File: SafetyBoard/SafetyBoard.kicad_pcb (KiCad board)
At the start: 2 copper layers, 169 parts, among them J1 ESTOP/SDC switch, J10 Dash, J11 BBC, J12 614004135023, J13 RTD B, J14 Brakelight, J15 SHOCK/WHEEL SNSR, J16 footwell, J18 AMP, J19 39306207, J2 SDC OUT, J3 ACCU, J4 12v EXP, J5 PWR IN, J6 24v EXP, J7 5v EXP, J8 Current Sensor, J9 TSSI, K1 G6B-2214P-US DC12, K2 G6B-2214P-US DC12, K3 G6B-2214P-US DC12, Q1 IRLIZ44N NMOS, Q2 IRLIZ44N NMOS, Q3 IRLIZ44N NMOS, Q4 IRLIZ44N NMOS, Q5 PMOS IRF9540, Q6 PMOS IRF9540, Q7 PMOS IRF9540, SW1 SW_Push, SW2 SW_Push, SW3 SW_Push, U1 40106 Inverter, U2 4081 AND Gate, U3 LT1084-5.0, U4 LM393, U5 LM393, U6 4071 4 Channel 2 Input OR gate, U7 LM393, U8 LM555xN, U9 OKX-T/5-D12N-C

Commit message: silkscreen and some fuses or something
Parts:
- removed the D1 at (177.2, 82.0)
- removed the D5 at (271.4, 67.4)
- removed FL1: RGF48040A-001, DCDCfootprints:EMI Filter RGF48040A001
- added C27: 1u, Capacitor_SMD:C_0805_2012Metric, B.Cu at (186.5, 125.1)
- added C30: 1u, Capacitor_SMD:C_0805_2012Metric, B.Cu at (155.0, 142.5)
- added D2: D, Diode_SMD:D_0603_1608Metric, B.Cu at (140.3, 95.5)
- added D7: D, Diode_SMD:D_0603_1608Metric, B.Cu at (148.4, 78.2)
- added R55: ~, Resistor_SMD:R_0805_2012Metric, B.Cu at (154.7, 147.5)
- added R56: 10k, Resistor_SMD:R_0603_1608Metric, B.Cu at (120.0, 74.5)
- C26, C4, LED1, R22, R25, R26, R27, R35, R36, R37, R_Bypass1, R_Bypass2: moved to B.Cu
- D12: renamed from D10; moved to B.Cu
- D3: value RF01VM2S -> D; footprint Diode_SMD:D_0805_2012Metric -> Diode_SMD:D_0603_1608Metric; moved to B.Cu
- D4: value RF01VM2S -> ON when ok; footprint Diode_SMD:D_0805_2012Metric -> LED_THT:LED_D5.0mm
- F1, F5: value ~ -> 2A MAX
- F10, F3, F6, F7: value ~ -> 5A MAX
- F11: renamed from F12; value ~ -> 3A
- F4, F8, F9: value ~ -> 10A MAX
- Q2, Q3: moved to F.Cu
- R29: renamed from R28; moved to B.Cu
- R30: renamed from R29; moved to B.Cu
- R31: renamed from R30; moved to B.Cu
- R34: renamed from R33; moved to B.Cu
- R38: renamed from R40; moved to B.Cu
- R39: renamed from R41; moved to B.Cu
- R41: renamed from R45; moved to B.Cu
- R42: renamed from R46; moved to B.Cu
- R43: renamed from R47; moved to B.Cu
- R49: renamed from R54; moved to B.Cu
- U6: value 4071 4 Channel 2 Input OR gate -> CD4071BE OR Gate
- moved F1 490.8 mm to (191.1, 121.6), turned to 90 degrees
- moved H1 341.8 mm to (318.5, 132.4)
- moved H2 341.8 mm to (318.5, 140.0)
- moved H3 341.8 mm to (318.5, 147.5)
- moved H4 341.8 mm to (318.5, 155.1)
- moved H5 248.9 mm to (368.4, 72.9)
- moved H7 248.9 mm to (368.4, 88.8)
- moved H8 248.9 mm to (368.4, 96.7)
- moved H6 248.9 mm to (368.4, 80.8)
- moved F5 241.6 mm to (208.3, 129.2), turned to 90 degrees
- moved F2 206.5 mm to (196.4, 132.0), turned to -90 degrees
- moved R38 182.8 mm to (176.0, 86.3)
- moved R39 179.6 mm to (183.4, 95.0)
- moved R42 173.6 mm to (197.0, 86.3), turned to 90 degrees
- moved R27 171.8 mm to (141.2, 92.9), turned to 90 degrees
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- renumbered LED3 to BothThreshold1, C27 to C28, C32 to C29, C28 to C31, C29 to C32, C30 to C33, C31 to C34, D2 to D1, D11 to D10, D12 to D11, D6 to D5, D7 to D6, D9 to D8, D8 to D9, F11 to F12, J16 to J13, J13 to J14, J14 to J15, J15 to J16, J19 to J17, LED2 to OutOfRange1, R34 to R28, R31 to R32, R32 to R33, R42 to R40, R49 to R44, R50 to R45, R51 to R46, R52 to R47, R53 to R48, R55 to R50, R56 to R51, R57 to R52, R58 to R53, R59 to R54
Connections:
- C20 pad 1: Net-(FL1-CASE) -> /24V
- C21 pad 1: Net-(FL1-VOUT(+)_) -> /24V
- C22 pad 1: Net-(FL1-VOUT(+)_) -> /24V
- D3 pad 1: Net-(D3-K) -> Net-(D2-K)
- D3 pad 2: /LATCH/bms_imd_latch_only -> Net-(D3-A)
- D4 pad 1: Net-(D3-K) -> GND
- F1 pad 1: +12V -> /12V
- F1 pad 2: /12V -> +12V
- J13 pad 4: unconnected-(J16-Pad4) -> /CCM Helper/CCM3v3
- J17 pad 10: unconnected-(J19-Pad10) -> /CCM Helper/24V
- J17 pad 11: unconnected-(J19-Pad11) -> /CCM Helper/RTDB
- J17 pad 12: /CCM Helper/CCMGND -> GND
- J17 pad 13: unconnected-(J19-Pad13) -> /CCM Helper/5V
- J17 pad 19: unconnected-(J19-Pad19) -> /CCM Helper/Brakelight
- J17 pad 20: /CCM Helper/Brakelight -> /CCM Helper/12V
- J17 pad 4: /CCM Helper/24V -> /CCM Helper/CCMGND
- J2 pad 1: Net-(J1-Pin_2) -> unconnected-(J2-Pin_1-Pad1)
- K1 pad 3: /LATCH/bms_imd_latch_only -> /LATCH/GVLM_OUTPUT
- K1 pad 4: /LATCH/GVLM_OUTPUT -> /LATCH/bms_imd_latch_only
- K2 pad 3: Net-(K2-Pad3) -> /LATCH/bms_imd_latch_only
- K2 pad 4: /LATCH/bms_imd_latch_only -> Net-(K2-Pad4)
- K3 pad 4: Net-(K2-Pad3) -> Net-(K2-Pad4)
- PS1 pad 1: Net-(FL1-VOUT(+)_) -> /24V
- PS1 pad 5: unconnected-(PS1-CURRENT_LIMIT_(OCP)_ADJUST-Pad5) -> Net-(PS1-CURRENT_LIMIT_(OCP)_ADJUST)
- PS1 pad 9: Net-(FL1-VOUT(+)_) -> /24V
- Q2 pad 2: GND -> Net-(D3-A)
- Q2 pad 3: Net-(D4-A) -> GND
- Q3 pad 1: Net-(D3-K) -> Net-(D2-K)
- R26 pad 2: Net-(D4-A) -> Net-(D3-A)
- R28 pad 1: Net-(D3-K) -> Net-(D2-K)
- R30 pad 1: Net-(D3-K) -> Net-(D2-K)
- R30 pad 2: Net-(D5-A) (its old number) -> Net-(D4-A)
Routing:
- net +12V: track 35.0 -> 262.4 mm, vias 0 -> 15
- net /CCM Helper/12V: track 0.00 -> 185.9 mm
- net Net-(J1-Pin_2): track 0.00 -> 174.9 mm, vias 0 -> 10
- net Net-(J3-Pin_1): track 0.00 -> 169.2 mm, vias 0 -> 5
- net Net-(D2-K): track 0.00 -> 137.1 mm, vias 0 -> 1
- net /TSSI/GLV: track 0.00 -> 123.2 mm, vias 0 -> 3
- net /BSPD/B_IN: track 0.00 -> 74.3 mm, vias 0 -> 2
- net /5V: track 0.00 -> 72.8 mm, vias 0 -> 1
- net /CCM Helper/CCM fdbk: track 0.00 -> 66.0 mm, vias 0 -> 1
- net /TSSI/GREEN_LED: track 0.00 -> 65.8 mm
- net /LATCH/bspd_reset: track 0.00 -> 65.6 mm, vias 0 -> 2
- net /CCM Helper/24V: track 0.00 -> 63.4 mm
- net /CCM Helper/CCMGND: track 0.00 -> 62.4 mm
- net /24V: track 0.00 -> 61.7 mm
- net /LATCH/bms_reset: track 0.00 -> 60.4 mm, vias 0 -> 2
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- added copper zone on In2.Cu, net +12V
- added copper zone on F.Cu, net /12V
- added copper zone on In2.Cu, net /12V
- added copper zone on In2.Cu, net /24V
- added copper zone on In1.Cu, net /CCM Helper/CCMGND
- added copper zone on In2.Cu, net /TSSI/GLV
- added copper zone on In1.Cu, net GND
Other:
- board outline added: 157 x 104.8 mm
- copper layers 2 -> 4
- board text added: "5V"
- board text added: "<SDC/Latch"
- board text added: "Brake Threshold"
- board text added: "CCM"
- board text added: "Current Threshold"
- board text added: "FootWell"
- board text added: "GND"
- board text added: "Open Circuit"
- board text added: "Pin 1"
- board text added: "SDC ^"
- board text added: "Short Circuit"

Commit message: I think think this is final but need to defuck the BOM
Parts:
- added J2: TS ON SW, 0footprints:Molex_Mini-Fit_Jr_5566-02A_2x01_P4.20mm_Vertical, F.Cu at (155.6, 66.0)
- F2: value ~ -> 5A MAX
- J1: value ESTOP/SDC switch -> Estop
- R17: renamed from R16; moved to B.Cu
- brkErr1: renamed from LED1; moved to F.Cu
- moved H2 343.6 mm to (3.27, 3.27)
- moved H4 246.9 mm to (71.6, 158.0)
- moved H1 121.5 mm to (217.3, 65.0)
- moved J16 8.77 mm to (70.9, 149.8), turned to 90 degrees
- moved F1 5.28 mm to (191.3, 126.9)
- moved F5 0.37 mm to (207.9, 129.2)
- moved Q4 0.37 mm to (218.6, 119.0)
- moved R34 0.24 mm to (212.2, 108.8)
- renumbered J9 to J10, J10 to J11, J11 to J12, J12 to J13, J13 to J14, J14 to J15, J15 to J16, J16 to J17, J17 to J18, J18 to J19, J2 to J3, J3 to J4, J4 to J5, J5 to J6, J6 to J7, J7 to J8, J8 to J9, R56 to R12, R12 to R13, R13 to R14, R14 to R15, R15 to R16, R17 to R18, R18 to R19, R19 to R20, R20 to R21, R21 to R22, R22 to R23, R23 to R24, R24 to R25, R25 to R26, R26 to R27, R27 to R28, R28 to R29, R29 to R30, R30 to R31, R31 to R32, R32 to R33, R33 to R34, R34 to R35, R35 to R36, R36 to R37, R37 to R38, R38 to R39, R39 to R40, R40 to R41, R41 to R42, R42 to R43, R43 to R44, R44 to R45, R45 to R46, R46 to R47, R47 to R48, R48 to R49, R49 to R50, R55 to R51, R50 to R52, R51 to R53, R52 to R54, R53 to R55, R54 to R56, R_Bypass1 to SchmittDis1, R_Bypass2 to schmittEN1
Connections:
- J3 pad 2: Net-(J1-Pin_2) -> Net-(J2-Pin_2)
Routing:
- net Net-(J1-Pin_2): track 174.9 -> 13.9 mm, vias 10 -> 0
- net Net-(J2-Pin_2): track 0.00 -> 158.6 mm
- net +12V: track 262.4 -> 297.3 mm, vias 15 -> 10
- net /5V: track 72.8 -> 58.8 mm, vias 1 -> 0
- net Net-(Q4-G): track 0.00 -> 12.5 mm
- net /CCM Helper/12V: track 185.9 -> 179.4 mm
- net Net-(J4-Pin_1): track 169.2 -> 164.5 mm
- net /CCM Helper/Brakelight: track 12.7 -> 8.02 mm
- net /12V: track 37.1 -> 37.9 mm, vias 2 -> 0
- net Net-(brkErr1-A): vias 0 -> 1
- net GND: vias 51 -> 53
- net /TSSI/GLV: vias 3 -> 2
- net /BSPD/BSPD_FAULT: vias 2 -> 1
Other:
- board text added: "(TSSI)"
- board text added: "+12v +12v"
- board text added: "12V"
- board text added: "12V IN 10A MAX"
- board text added: "12v"
- board text added: "12v EXP"
- board text added: "< ACCU"
- board text added: "BMS"
- board text added: "BSPD"
- board text added: "CCM 24v"
- board text added: "CTRL (GND)"
- board text added: "DNC SDC ^"
- board text added: "Fault LEDs"
- board text added: "Green"
- board text added: "IMD"
- board text added: "LEDs"
- board text added: "Latch & SDC"
- board text added: "ONLY populate EN or DIS NOT BOTH"
- board text added: "RED"
- board text added: "Reset Switch"
- board text added: "TSSI"
- board text added: "USB"
- board text added: "X"
- board text added: "^ Latch points up ^"
- board text added: "sig"
- board text removed: "<SDC/Latch"
- board text removed: "Pin 1"
- board text removed: "SDC ^"

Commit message: updates I think
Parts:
- removed H5, H6, H7, H8: MountingHole, MountingHole:MountingHole_3.2mm_M3
- added C35: 22uf, Capacitor_SMD:C_2220_5750Metric_Pad1.97x5.40mm_HandSolder, B.Cu at (149.5, 133.9)
- C14, C15, C18, C19, C20, C27, C30: value 1u -> 1uF
- C16, C25, C29: value 330uF -> 22uf
- C21: footprint Capacitor_SMD:C_2220_5750Metric_Pad1.97x5.40mm_HandSolder -> Capacitor_THT:CP_Radial_D12.5mm_P5.00mm; moved to F.Cu
- C23, C28: value 22uF -> 22uf; footprint Capacitor_SMD:C_0805_2012Metric -> Capacitor_SMD:C_2220_5750Metric_Pad1.97x5.40mm_HandSolder
- C24: value 10u -> 10uF
- C26: value 10n -> 10nF
- F11: value 3A -> 3A MAX
- J11: value Dash -> ACCU; footprint footprints:Molex_Mini-Fit_Jr_5566-06A_2x03_P4.20mm_Vertical -> 0footprints:Molex_Mini-Fit_Jr_5566-04A_2x02_P4.20mm_Vertical
- moved H3 114.5 mm to (204.4, 157.4)
- moved H2 113.1 mm to (70.0, 94.7), turned to 90 degrees
- moved C25 43.2 mm to (141.7, 142.7), turned to -90 degrees
- moved J14 25.8 mm to (97.2, 153.0), turned to -90 degrees
- moved C21 24.9 mm to (119.7, 128.2), turned to 90 degrees
- moved C28 13.9 mm to (141.7, 134.3), turned to 90 degrees
- moved J11 9.07 mm to (175.4, 120.5), turned to 90 degrees
- moved J6 8.82 mm to (109.5, 130.0), turned to 180 degrees
- moved C23 8.30 mm to (184.9, 137.8)
- moved F9 8.23 mm to (116.9, 145.1)
- moved J2 5.57 mm to (155.6, 71.5), turned to 180 degrees
- moved J1 5.41 mm to (144.2, 72.2), turned to 180 degrees
- moved F8 5.37 mm to (116.8, 136.0)
- moved J7 4.85 mm to (115.0, 151.0)
- moved F4 3.49 mm to (116.6, 157.4)
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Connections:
- C25 pad 1: /12V -> Net-(PS1-SENSE+)
- F2 pad 1: +12V -> /12V
- F2 pad 2: /12V -> +12V
- F6 pad 1: Net-(J4-Pin_1) -> /12V
- F6 pad 2: /12V -> Net-(J4-Pin_1)
- J11 pad 2: GND -> /LATCH/BSPDfault_LED
- J11 pad 3: GND -> /LATCH/BMSfault_LED
- J11 pad 4: /LATCH/BMSfault_LED -> /LATCH/IMDfault_LED
- J14 pad 1: /CCM Helper/5V -> unconnected-(J14-Pad1)
- J14 pad 10: /CCM Helper/CCMGND -> /CCM Helper/APPS1 IN
- J14 pad 12: /CCM Helper/CCMGND -> /CCM Helper/BPS2 IN
- J14 pad 13: /CCM Helper/CCMGND -> /CCM Helper/BPS1 IN
- J14 pad 14: unconnected-(J14-Pad14) -> /CCM Helper/5V
- J14 pad 2: /CCM Helper/BPS1 IN -> /CCM Helper/CCMGND
- J14 pad 3: /CCM Helper/BPS2 IN -> /CCM Helper/CCMGND
- J14 pad 5: /CCM Helper/APPS1 IN -> /CCM Helper/CCMGND
- J14 pad 6: /CCM Helper/APPS2 IN -> /CCM Helper/CCMGND
- J14 pad 7: unconnected-(J14-Pad7) -> /CCM Helper/5V
- J14 pad 8: /CCM Helper/5V -> unconnected-(J14-Pad8)
- J14 pad 9: /CCM Helper/CCMGND -> /CCM Helper/APPS2 IN
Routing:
- net /24V: track 61.7 -> 8.50 mm
- net Net-(PS1-SENSE+): track 57.5 -> 84.9 mm
- net Net-(J7-Pin_1): track 26.3 -> 13.4 mm
- net /CCM Helper/24V: track 63.4 -> 53.6 mm
- net Net-(J6-Pin_1): track 23.6 -> 15.1 mm
- net /LATCH/BMSfault_LED: track 34.3 -> 40.7 mm
- net /LATCH/GVLM_OUTPUT: track 25.0 -> 19.6 mm
- net /CCM Helper/CCMGND: track 62.4 -> 59.5 mm
- net Net-(J2-Pin_2): track 158.6 -> 156.4 mm
- net /BSPD/B_IN: track 74.3 -> 72.1 mm
- net /CCM Helper/5V: track 48.0 -> 50.0 mm
- net /CCM Helper/Wheel/Shock4 IN: track 3.51 -> 4.40 mm
- net /CCM Helper/Wheel/Shock3 IN: track 3.57 -> 4.40 mm
- net /LATCH/IMDfault_LED: track 53.6 -> 52.8 mm, vias 1 -> 2
- net /CCM Helper/Wheel/Shock1 IN: track 3.65 -> 4.37 mm
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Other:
- board text added: "DASH LEDs"
- board text removed: "LEDs"
- board text removed: "dont forget LDO caps!"
- board text removed: "dont forget caps"

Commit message: silkscreen finish touches
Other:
- board text added: "Safety Board By: Gabriel Schoene"

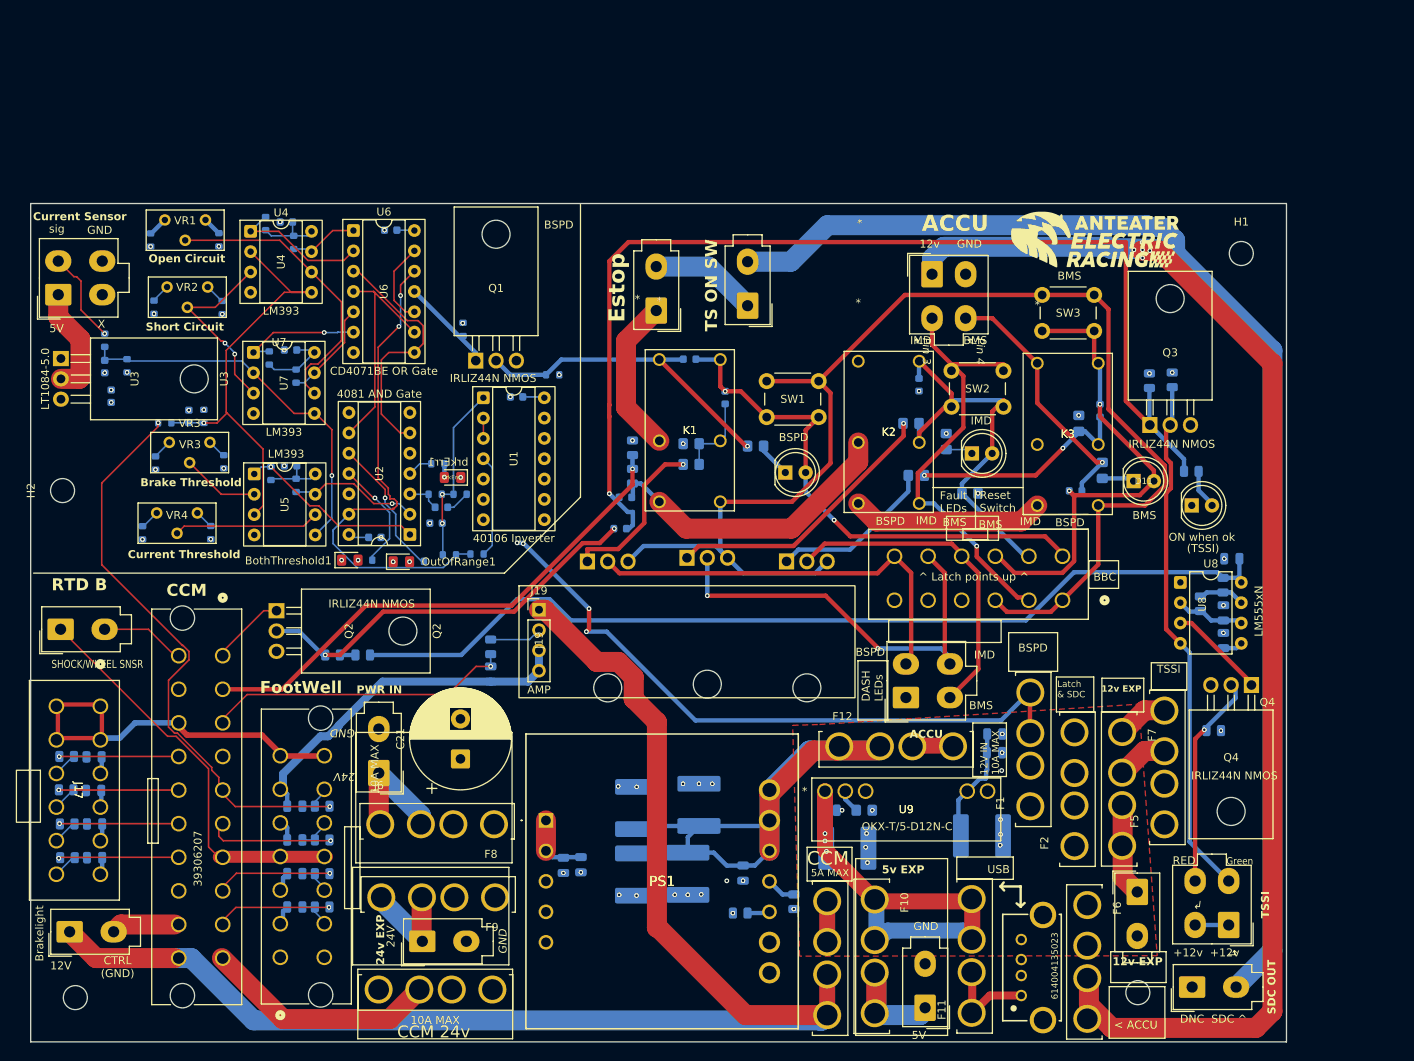
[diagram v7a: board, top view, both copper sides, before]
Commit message: Right-side realignment
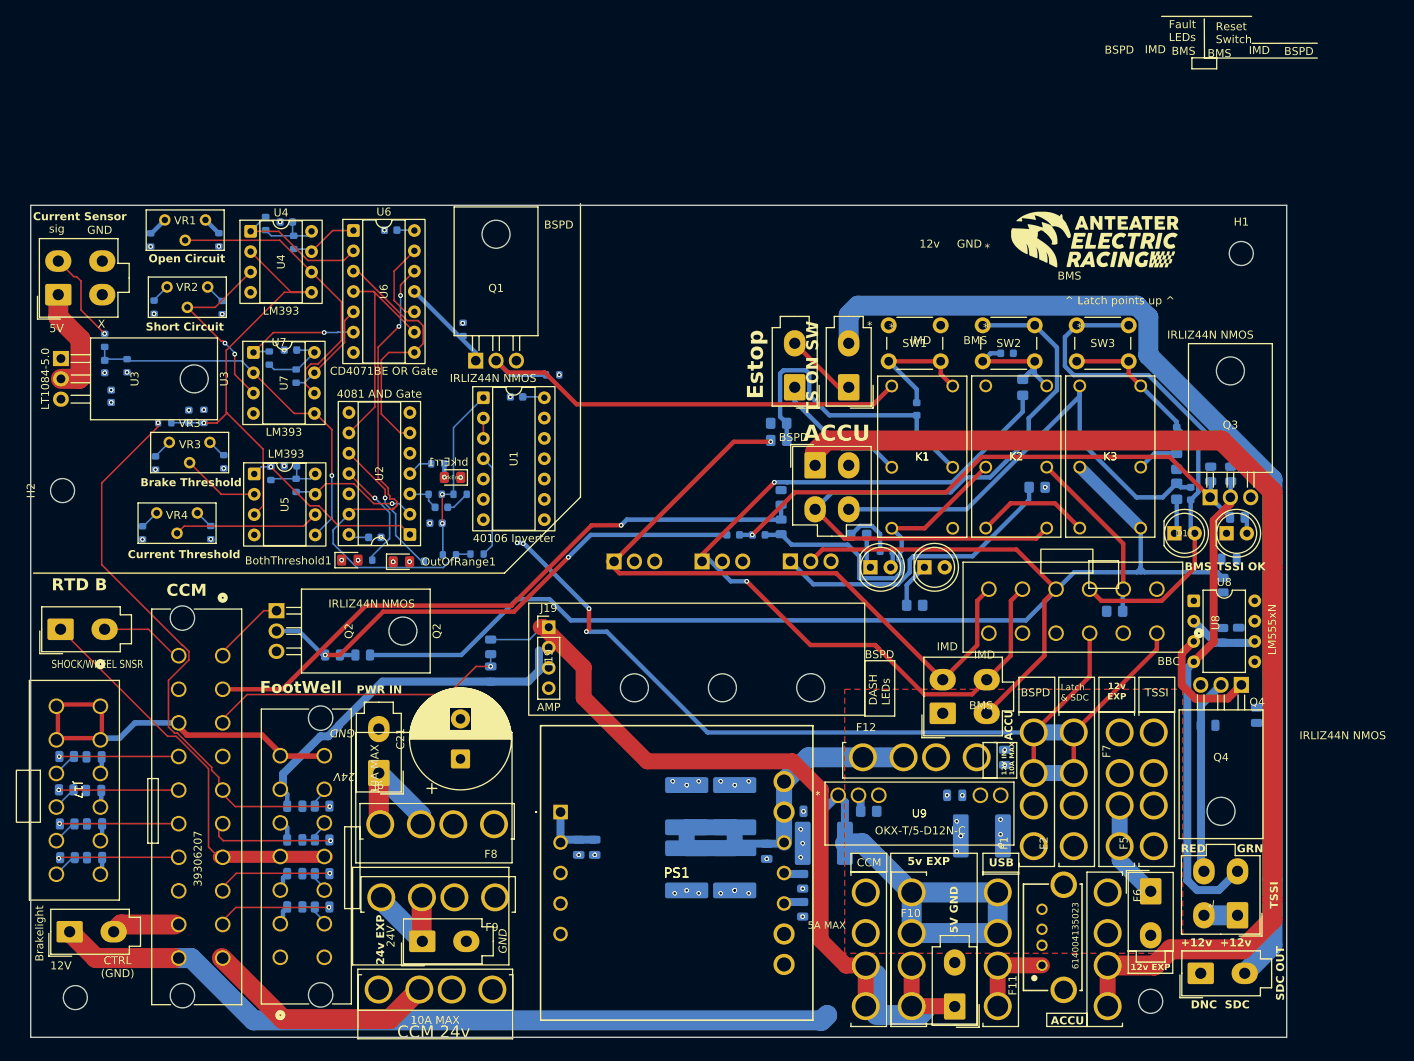
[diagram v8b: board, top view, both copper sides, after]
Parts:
- moved D7 34.4 mm to (173.0, 102.2)
- moved K1 29.2 mm to (181.2, 99.3)
- moved J4 28.0 mm to (164.1, 91.5)
- moved D5 24.0 mm to (176.8, 84.5)
- moved R40 23.3 mm to (201.5, 109.8), turned to 180 degrees
- moved R41 20.8 mm to (176.5, 109.0), turned to 0 degrees
- moved J1 19.8 mm to (161.5, 81.8)
- moved R28 19.6 mm to (159.8, 99.2)
- moved R30 19.6 mm to (159.8, 95.5)
- moved D2 17.3 mm to (157.0, 100.2)
- moved R38 17.0 mm to (169.5, 100.2)
- moved SW1 16.8 mm to (173.2, 74.0)
- moved J2 16.2 mm to (168.2, 81.8)
- moved K2 16.2 mm to (193.0, 99.2)
- moved D6 15.9 mm to (171.0, 104.2)
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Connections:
- C13 pad 1: /TSSI/GLV -> +12V
- R26 pad 1: /TSSI/GLV -> +12V
- R32 pad 1: /TSSI/GLV -> +12V
- R33 pad 1: /TSSI/GLV -> +12V
- R35 pad 1: /TSSI/GLV -> +12V
- U8 pad 8: /TSSI/GLV -> +12V
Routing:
- net /TSSI/GLV: track 123.2 -> 4.20 mm, vias 2 -> 0
- net Net-(D2-K): track 137.1 -> 70.5 mm
- net /IMD Fault: track 53.0 -> 105.3 mm, vias 1 -> 0
- net +12V: track 297.3 -> 346.7 mm
- net /12V: track 37.9 -> 0.00 mm, vias 0 -> 6
- net Net-(PS1-SENSE+): track 84.9 -> 47.5 mm
- net /BMS FAULT: track 32.1 -> 60.6 mm, vias 1 -> 0
- net Net-(D5-A): track 10.3 -> 38.2 mm
- net /BSPD/BSPD_FAULT: track 40.6 -> 66.4 mm, vias 1 -> 0
- net /LATCH/imd_reset: track 49.8 -> 74.5 mm
- net Net-(J2-Pin_2): track 156.4 -> 132.0 mm
- net Net-(J4-Pin_1): track 164.4 -> 143.6 mm, vias 5 -> 0
- net Net-(Q7-G): track 20.8 -> 37.9 mm
- net /LATCH/bspd_reset: track 65.6 -> 81.6 mm, vias 2 -> 0
- net Net-(Q6-G): track 35.0 -> 50.5 mm
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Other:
- board size 157 x 104.8 mm -> 157 x 104 mm
- board text added: "ACCU"
- board text added: "DNC SDC"
- board text added: "GRN"
- board text added: "TSSI OK"
- board text removed: "(TSSI)"
- board text removed: "< ACCU"
- board text removed: "DNC SDC ^"
- board text removed: "Green"
